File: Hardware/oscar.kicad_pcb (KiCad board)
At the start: 2 copper layers, 80 x 110 mm, 49 parts, among them J1 SWD_Header, J2 ChannelA_In, J3 ChannelB_In, J4 ChannelC_In, J5 ChA_Buff_Out, J6 ChB_Buff_Out, J7 ChC_Buff_Out, J8 MIDI_In, J9 Eurorack_16_pin_power, SW1 Left_Encoder, SW2 Right_Encoder, SW3 SW_Push_Dual, U1 STM32F446RETx, U2 ILI9341_SPI, U3 MCP6004, U4 TL074, U5 LM1117-3.3, Y1 Crystal

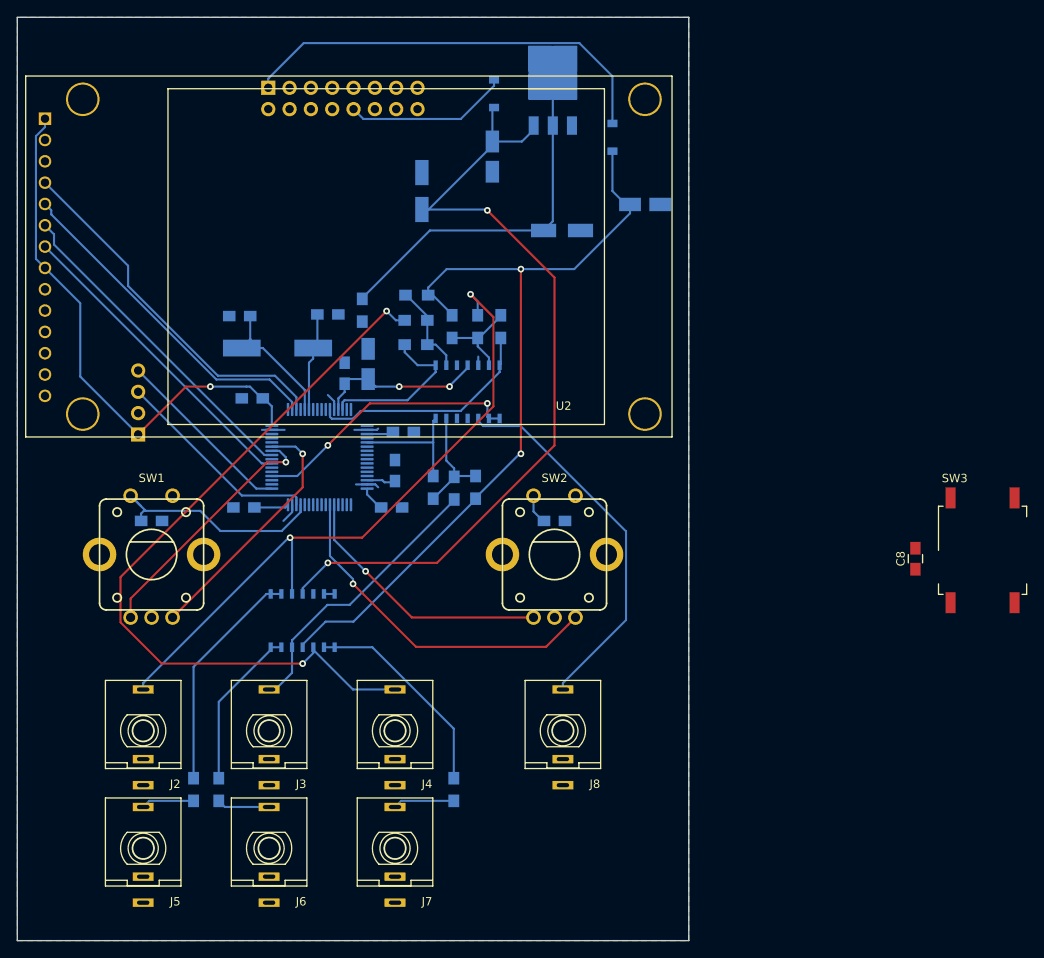
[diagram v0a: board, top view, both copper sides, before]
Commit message: Better scaling for horizontal zoom; 4 layer board updates
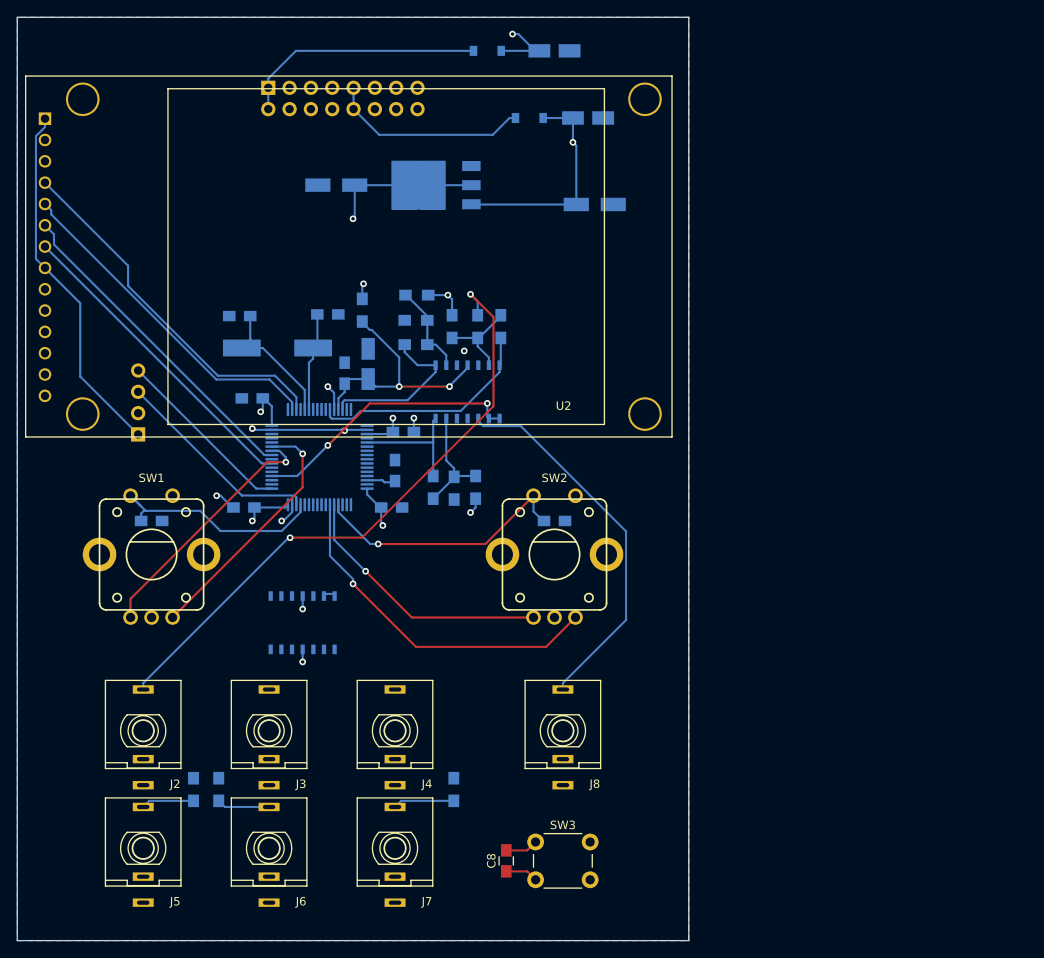
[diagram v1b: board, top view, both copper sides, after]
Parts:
- SW3: value SW_Push_Dual -> SW_Push; footprint Buttons_Switches_SMD:SW_MEC_5GSH9 -> Buttons_Switches_THT:SW_PUSH_6mm
- moved SW3 63.6 mm to (181.8, 148.2)
- moved C8 60.6 mm to (178.2, 150.5)
- moved C14 27.4 mm to (158.0, 70.0), turned to 180 degrees
- moved C13 21.2 mm to (184.0, 54.0)
- moved C11 20.7 mm to (188.8, 72.3), turned to 0 degrees
- moved D2 18.1 mm to (176.0, 54.0), turned to 0 degrees
- moved U5 17.9 mm to (169.9, 70.0), turned to 180 degrees
- moved C12 12.3 mm to (188.0, 62.0), turned to 0 degrees
- moved D1 5.10 mm to (181.0, 62.0), turned to 180 degrees
- turned U4 to 180 degrees
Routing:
- net Net-(J4-Pad3): track 91.0 -> 0.00 mm, vias 2 -> 0
- net VEE: track 99.0 -> 17.8 mm, vias 2 -> 4
- net VCC: track 99.1 -> 29.0 mm
- net +3V3: track 119.3 -> 84.3 mm, vias 1 -> 6
- net Net-(J3-Pad3): track 33.8 -> 0.85 mm
- net R_ENC_BTN: track 3.59 -> 31.7 mm, vias 0 -> 1
- net Net-(R10-Pad2): track 27.3 -> 0.00 mm
- net Net-(R12-Pad2): track 25.4 -> 0.00 mm
- net -12V: track 51.1 -> 29.5 mm
- net Net-(R11-Pad2): track 19.4 -> 1.27 mm
- net GND: track 13.8 -> 27.4 mm, vias 0 -> 7
- net +3.3VA: track 19.9 -> 29.6 mm
- net Net-(J2-Pad3): track 80.6 -> 73.8 mm
- net +12V: track 19.6 -> 23.9 mm
- net NRST: track 0.00 -> 3.91 mm
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- added copper zone on PWR, net +3V3
- added copper zone on GND, net GND
- added copper zone on PWR, net VCC
- added copper zone on PWR, net VEE
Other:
- copper layers 2 -> 4
- board text added: "VCC"
- board text added: "VEE"

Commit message: MIDI uses ring buffer instead of queu and added clock
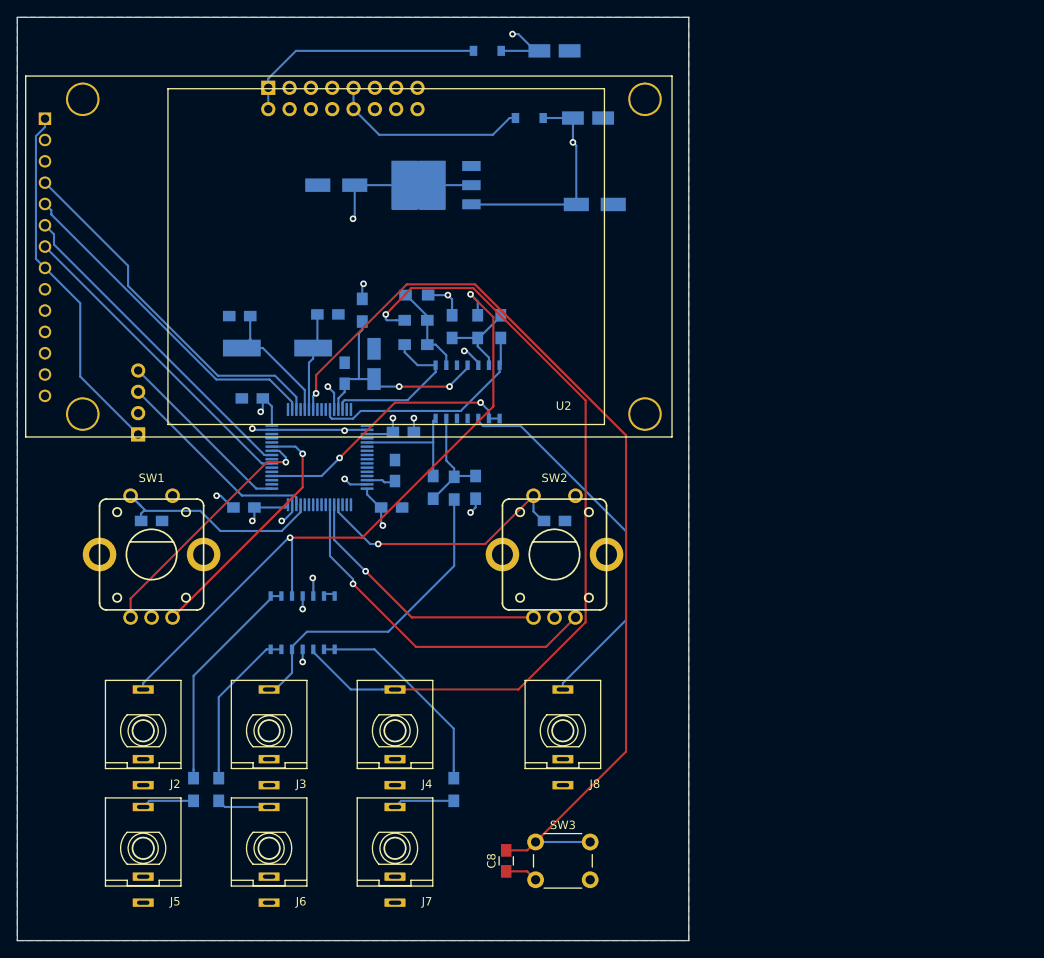
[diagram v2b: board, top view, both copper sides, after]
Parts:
- moved C15 0.70 mm to (162.5, 91.3)
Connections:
- U4 pad 1: Net-(R10-Pad2) -> Net-(R12-Pad2)
- U4 pad 10: Net-(J4-Pad3) -> Net-(J2-Pad3)
- U4 pad 12: Net-(J3-Pad3) -> GND
- U4 pad 13: Net-(R11-Pad2) -> Net-(U4-Pad13)
- U4 pad 14: Net-(R11-Pad2) -> Net-(U4-Pad13)
- U4 pad 2: Net-(R10-Pad2) -> Net-(R12-Pad2)
- U4 pad 3: Net-(J2-Pad3) -> Net-(J4-Pad3)
- U4 pad 5: GND -> Net-(J3-Pad3)
- U4 pad 6: Net-(U4-Pad6) -> Net-(R11-Pad2)
- U4 pad 7: Net-(U4-Pad6) -> Net-(R11-Pad2)
- U4 pad 8: Net-(R12-Pad2) -> Net-(R10-Pad2)
- U4 pad 9: Net-(R12-Pad2) -> Net-(R10-Pad2)
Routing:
- net NRST: track 3.91 -> 116.4 mm, vias 0 -> 1
- net Net-(J4-Pad3): track 0.00 -> 97.9 mm, vias 0 -> 1
- net Net-(J3-Pad3): track 0.85 -> 38.0 mm
- net Net-(R10-Pad2): track 0.00 -> 26.8 mm
- net Net-(R12-Pad2): track 0.00 -> 25.3 mm
- net Net-(R11-Pad2): track 1.27 -> 19.5 mm
- net GND: track 27.4 -> 35.0 mm, vias 7 -> 9
- net Net-(J2-Pad3): track 73.8 -> 80.9 mm
- net +3.3VA: track 29.6 -> 27.0 mm
- net Net-(U4-Pad13): track 0.00 -> 1.27 mm

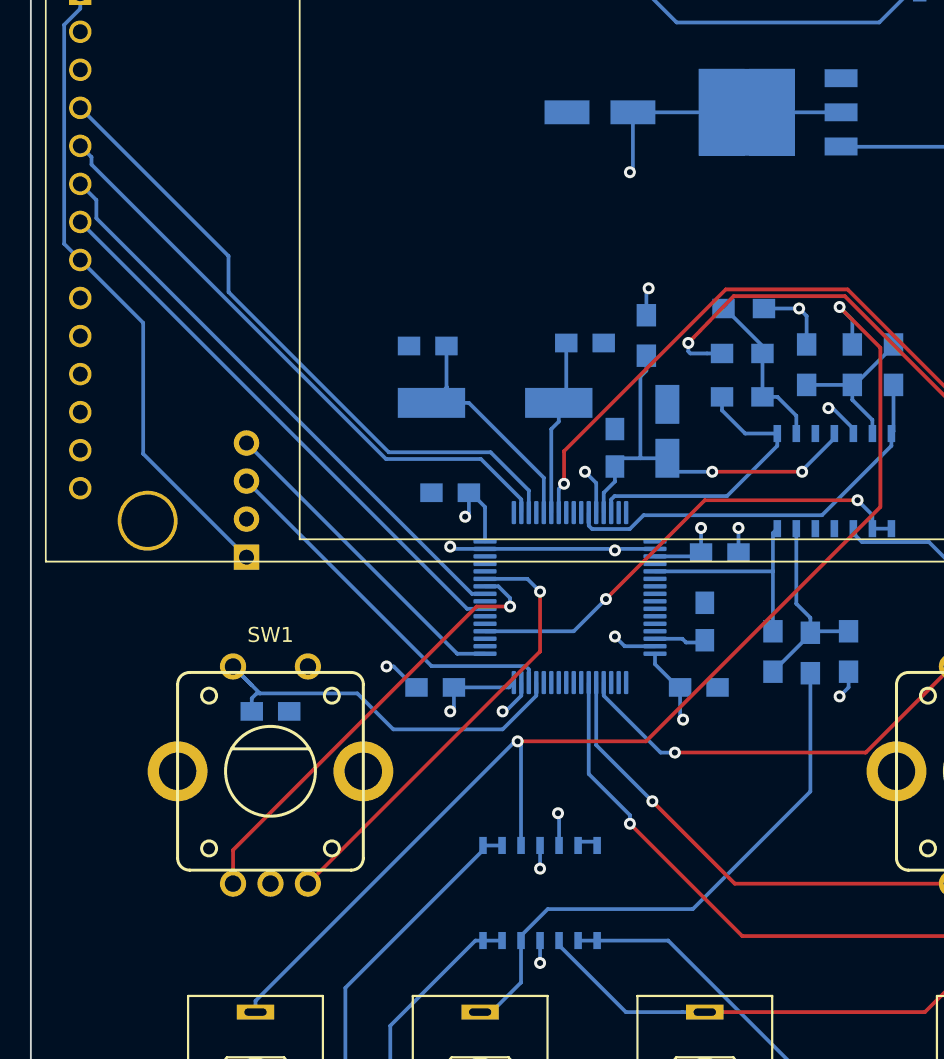
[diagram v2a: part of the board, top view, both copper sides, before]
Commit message: Added LCD Solder pads
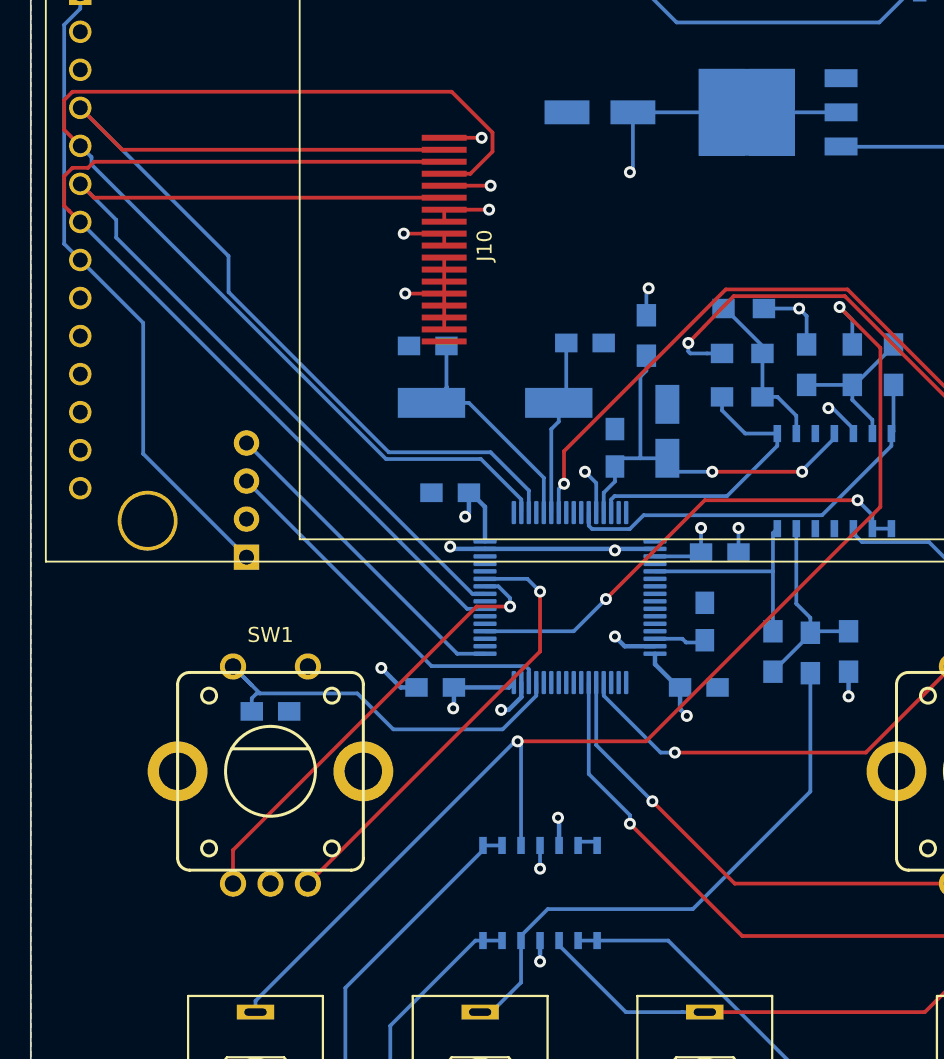
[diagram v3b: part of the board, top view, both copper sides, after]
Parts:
- added J10: LCD_Connector, Custom_Footprints:18x0.8mmLCDConnector, F.Cu at (147.6, 71.7)
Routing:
- net LCD_DC: track 40.4 -> 79.0 mm
- net LCD_SCK: track 37.7 -> 67.0 mm
- net LCD_RESET: track 43.4 -> 68.9 mm
- net LCD_MOSI: track 39.1 -> 63.7 mm
- net GND: track 35.0 -> 52.2 mm, vias 9 -> 13
- net +3V3: track 84.3 -> 87.4 mm, vias 6 -> 7

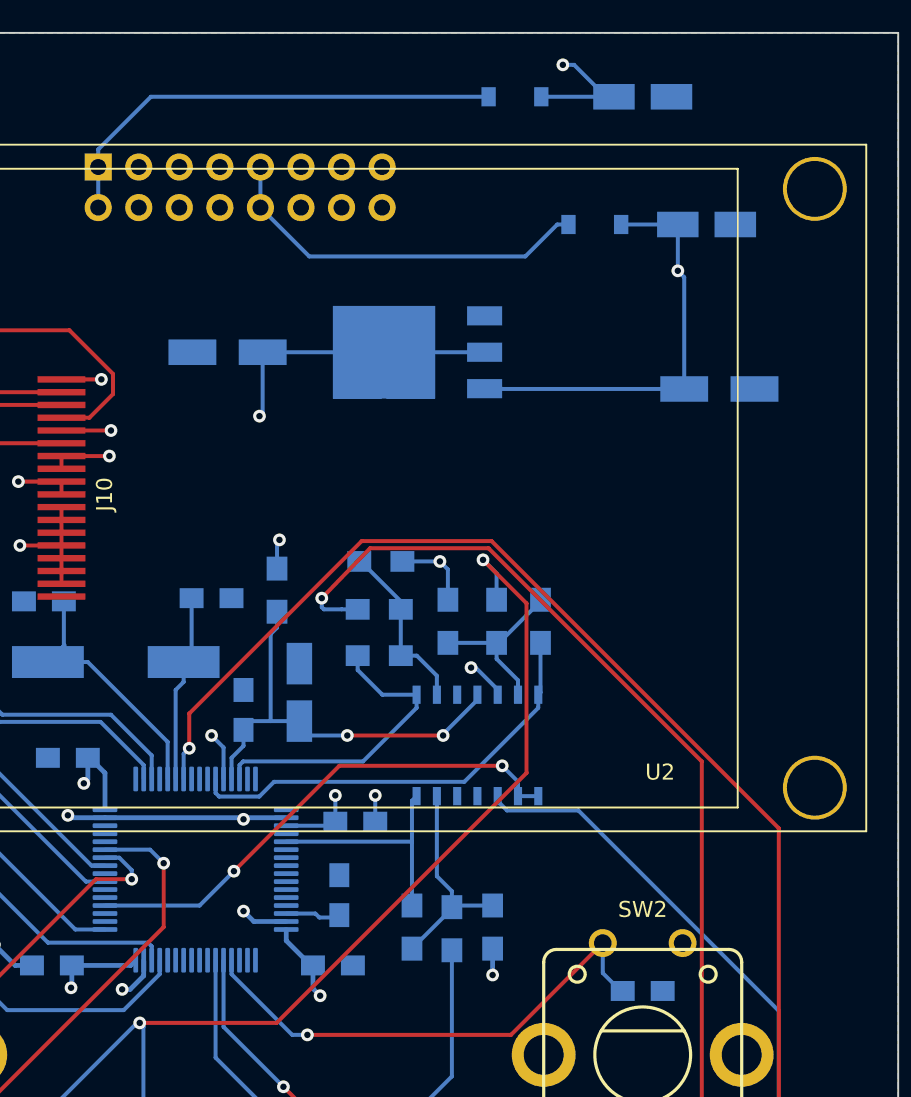
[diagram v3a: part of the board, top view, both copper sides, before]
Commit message: increased size of power traces
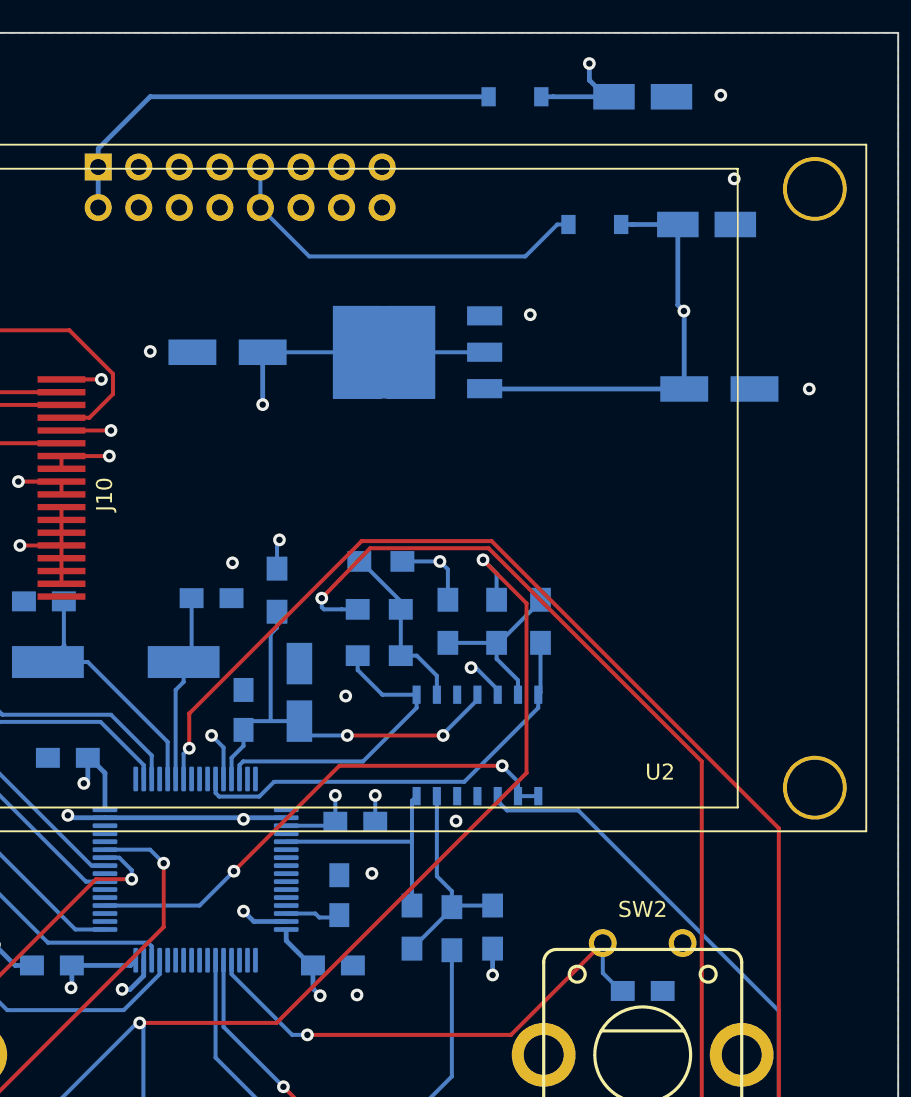
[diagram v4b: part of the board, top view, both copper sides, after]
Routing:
- net VEE: track 17.6 -> 16.6 mm
- net VCC: track 28.9 -> 27.9 mm
- net +3V3: track 87.4 -> 86.6 mm
- net GND: vias 13 -> 23
